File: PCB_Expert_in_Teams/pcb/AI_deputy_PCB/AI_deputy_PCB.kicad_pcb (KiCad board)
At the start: 2 copper layers, 154 parts, among them IC1 DA7280-00FVC, IC2 DA7281-00FVC, IC3 DA7282-00FVC, IC4 IS31AP2005-SLS2-TR, IC5 IS31AP2005-SLS2-TR, IC6 LM25576QMH_NOPB, IC7 CYPD3177-24LQXQ, IC8 FT231XS-R, IC9 PCM5102APWR, J1 Piezo Electric, J10 OUTPUT Haptic B (Neck R), J11 OUTPUT Haptic C (Back), J13 Conn_01x02_Socket, J14 Conn_01x02_Socket, J15 Conn_01x04_Socket, J16 Conn_01x01_Pin, J17 Conn_01x01_Pin, J18 Conn_01x03_Socket, J19 Conn_01x01_Pin, J2 2171790001, J20 Conn_01x01_Pin, J3 Haptic Power and GND, J4 UART, J5 JST CONN from MCU, J6 JTAG, J8 Conn_01x04_Socket, J9 OUTPUT Haptic A (Neck L), Q1 NMOS IRLZ44NPBF, Q2 DMP3098LSD-13, Q4 DMP3098LSD-13, U2 ESP32-WROOM-32UE

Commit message: finished PCB design and gerbers are in directory
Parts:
- removed the D1 at (207.7, 147.9)
- removed the D1 at (101.7, 91.1)
- removed J15: Conn_01x04_Socket, Connector_JST:JST_XH_S4B-XH-A_1x04_P2.50mm_Horizontal
- removed J3: Haptic Power and GND, Connector_JST:JST_XH_S2B-XH-A_1x02_P2.50mm_Horizontal
- removed J5: JST CONN from MCU, Connector_JST:JST_XH_S3B-XH-A_1x03_P2.50mm_Horizontal
- removed J8: Conn_01x04_Socket, Connector_JST:JST_XH_S4B-XH-A-1_1x04_P2.50mm_Horizontal
- removed JP1, JP2: SolderJumper_2_Open, Jumper:SolderJumper-2_P1.3mm_Open_RoundedPad1.0x1.5mm
- removed Q1: NMOS IRLZ44NPBF, Package_TO_SOT_THT:TO-220-3_Horizontal_TabDown
- removed R39, R40: 100k, Resistor_SMD:R_0805_2012Metric_Pad1.20x1.40mm_HandSolder
- removed R53: 3.3k, Resistor_SMD:R_0805_2012Metric_Pad1.20x1.40mm_HandSolder
- removed the R8 at (101.7, 86.3)
- removed the R8 at (207.6, 142.0)
- added C43: 0.1u, Capacitor_SMD:C_0805_2012Metric_Pad1.18x1.45mm_HandSolder, F.Cu at (105.8, 112.0)
- added C60: 10u, Capacitor_SMD:CP_Elec_4x5.4, F.Cu at (99.8, 111.0)
- added C61: 4u7, Capacitor_SMD:C_0805_2012Metric_Pad1.18x1.45mm_HandSolder, F.Cu at (108.0, 107.5)
- added C62: 100n, Capacitor_SMD:C_0805_2012Metric_Pad1.18x1.45mm_HandSolder, F.Cu at (178.1, 81.9)
- added D1: LED, LED_SMD:LED_0805_2012Metric_Pad1.15x1.40mm_HandSolder, F.Cu at (86.9, 86.1)
- added H1: MountingHole, MountingHole:MountingHole_3mm, F.Cu at (195.6, 140.7)
- added H2: MountingHole, MountingHole:MountingHole_3mm, F.Cu at (157.4, 89.7)
- added H3: MountingHole, MountingHole:MountingHole_3mm, F.Cu at (221.9, 85.3)
- added H4: MountingHole, MountingHole:MountingHole_3mm, F.Cu at (73.0, 84.3)
- added H5: MountingHole, MountingHole:MountingHole_3mm, F.Cu at (77.7, 131.3)
- added H6: MountingHole, MountingHole:MountingHole_3mm, F.Cu at (133.3, 125.6)
- added J12: Conn_01x01_Pin, TestPoint:TestPoint_Pad_4.0x4.0mm, F.Cu at (222.0, 103.0)
- added J7: Conn_01x01_Pin, TestPoint:TestPoint_Pad_4.0x4.0mm, F.Cu at (222.0, 112.0)
- added JP3: Jumper_3_Open, Jumper:SolderJumper-3_P1.3mm_Open_Pad1.0x1.5mm_NumberLabels, F.Cu at (130.5, 117.2)
- added JP4: Jumper_3_Open, Jumper:SolderJumper-3_P1.3mm_Open_Pad1.0x1.5mm_NumberLabels, F.Cu at (119.8, 104.0)
- added JP5: Jumper_3_Open, Jumper:SolderJumper-3_P1.3mm_Open_Pad1.0x1.5mm_NumberLabels, F.Cu at (113.2, 141.8)
- added JP6: Jumper_3_Open, Jumper:SolderJumper-3_P1.3mm_Open_Pad1.0x1.5mm_NumberLabels, F.Cu at (126.8, 141.8)
- added L1: 220u, Inductor_SMD:L_Wuerth_WE-PD-Typ-LS, F.Cu at (158.8, 106.5)
- added Q3: Q_NMOS_GDS_IRLZ44N, Package_TO_SOT_THT:TO-220-3_Horizontal_TabDown, F.Cu at (154.7, 133.8)
- added R8: 10k, Resistor_SMD:R_0805_2012Metric_Pad1.20x1.40mm_HandSolder, F.Cu at (91.8, 86.2)
- added S3: L101121MS02Q, EXT_AI_DEPUTY_Library:PWR_SW_L101021MS02Q, F.Cu at (216.0, 141.3)
- added S4: 430773034825, EXT_AI_DEPUTY_Library:430773034825, F.Cu at (143.5, 97.5)
- C46: value 100n -> 1u
- R1: value 3.3k -> 2.7k
- R41: value 10k -> 7.5k
- R47: value 68 -> 100
- R6: value 3.3k -> 10k
- moved R6 108.0 mm to (181.4, 81.8), turned to -90 degrees
- moved R46 95.3 mm to (122.0, 109.0), turned to 90 degrees
- moved R45 89.7 mm to (126.8, 109.0), turned to 90 degrees
- moved R44 84.3 mm to (131.2, 109.0), turned to 90 degrees
- moved J18 80.2 mm to (202.8, 77.7)
- moved C27 68.9 mm to (216.1, 122.8), turned to 90 degrees
- moved C36 58.9 mm to (211.1, 125.4), turned to 90 degrees
- moved C28 55.6 mm to (208.1, 115.9), turned to 90 degrees
- moved R15 53.5 mm to (208.1, 120.4), turned to 90 degrees
- moved R47 53.3 mm to (154.5, 140.2), turned to -90 degrees
- moved R50 52.0 mm to (196.8, 107.0), turned to -90 degrees
- moved C31 50.7 mm to (206.6, 128.9), turned to 0 degrees
- moved R1 50.1 mm to (117.0, 108.8), turned to 180 degrees
- moved C37 49.9 mm to (206.6, 125.4), turned to 90 degrees
- moved R3 49.7 mm to (158.2, 139.6)
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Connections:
- net +BATT renamed +VDC
- C46 pad 1: Net-(IC8-3V3OUT) -> +3V3
- C56 pad 1: Signal Right -> DAC_OUTR
- C57 pad 1: Signal Left -> DAC_OUTL
- IC8 pad 13: Net-(IC8-3V3OUT) -> +3V3
- IC8 pad 14: Net-(IC8-3V3OUT) -> Net-(IC8-RESET#)
- IC8 pad 19: Net-(IC8-CBUS3) -> unconnected-(IC8-CBUS3-Pad19)
- IC9 pad 11: GND -> Net-(IC9-FLT)
- IC9 pad 12: unconnected-(IC9-SCK-Pad12) -> GND
- IC9 pad 16: GND -> Net-(IC9-FMT)
- IC9 pad 17: MUTE -> Net-(IC9-XSMT)
- IC9 pad 18: +3V3 -> Net-(IC9-LDOO)
- R1 pad 1: +3V3 -> GND
- R1 pad 2: NIRQ -> Net-(IC9-XSMT)
- R41 pad 1: MUTE -> Net-(IC9-XSMT)
- R42 pad 2: Signal Right -> DAC_OUTR
- R43 pad 2: Signal Left -> DAC_OUTL
- R5 pad 2: SDA -> NIRQ
- R6 pad 2: SCL -> Net-(IC8-RESET#)
- U2 pad 10: Net-(JP2-A) -> ESPDACOUTL
- U2 pad 11: Net-(JP1-A) -> ESPDACOUTR
- U2 pad 31: PD_INT -> unconnected-(U2-IO19-Pad31)
- U2 pad 37: MUTE -> unconnected-(U2-IO23-Pad37)
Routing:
- net +3V3: track 435.4 -> 879.4 mm, vias 4 -> 19
- net GND: track 0.00 -> 295.8 mm, vias 0 -> 836
- net MCU PWM: track 0.00 -> 90.5 mm, vias 0 -> 2
- net +VDC: track 19.3 -> 100.7 mm
- net SCL: track 67.8 -> 137.7 mm, vias 4 -> 8
- net ESPDACOUTL: track 0.00 -> 65.4 mm, vias 0 -> 2
- net SDA: track 58.7 -> 123.9 mm, vias 5 -> 9
- net ESPDACOUTR: track 0.00 -> 63.0 mm, vias 0 -> 2
- net Signal Left: track 2.28 -> 53.9 mm
- net BOOT: track 9.87 -> 59.8 mm
- net USB_TX: track 7.69 -> 52.3 mm, vias 0 -> 2
- net Net-(Q3-D): track 0.00 -> 40.8 mm
- net NIRQ: track 70.7 -> 109.4 mm, vias 7 -> 9
- net USB_RX: track 7.34 -> 41.9 mm, vias 0 -> 2
- net +BATT: track 0.00 -> 32.7 mm
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- added copper zone on B.Cu, net GND
- added copper zone on F.Cu, net GND
- removed copper zone on F.Cu, net VDC_OUT
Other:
- board outline added: 175 x 71.2 mm
- board text added: "+"
- board text added: "-"
- board text added: "3V3"
- board text added: "3V3 Input Bypass reg."
- board text added: "AUDIO OUT L"
- board text added: "AUDIO OUT R"
- board text added: "BOOT"
- board text added: "BT_LINK"
- board text added: "Battery Input"
- board text added: "DAC"
- board text added: "ESP"
- board text added: "ESP32 JTAG"
- board text added: "ESP32 UART"
- board text added: "Haptic Neck Back"
- board text added: "Haptic Neck L"
- board text added: "Haptic Neck R"
- board text added: "Olfactory Output"
- board text added: "PD I2C"
- board text added: "PD OUT"
- board text added: "PWR SW"
- board text added: "RESET"
- board text added: "RX"
- board text added: "TX"

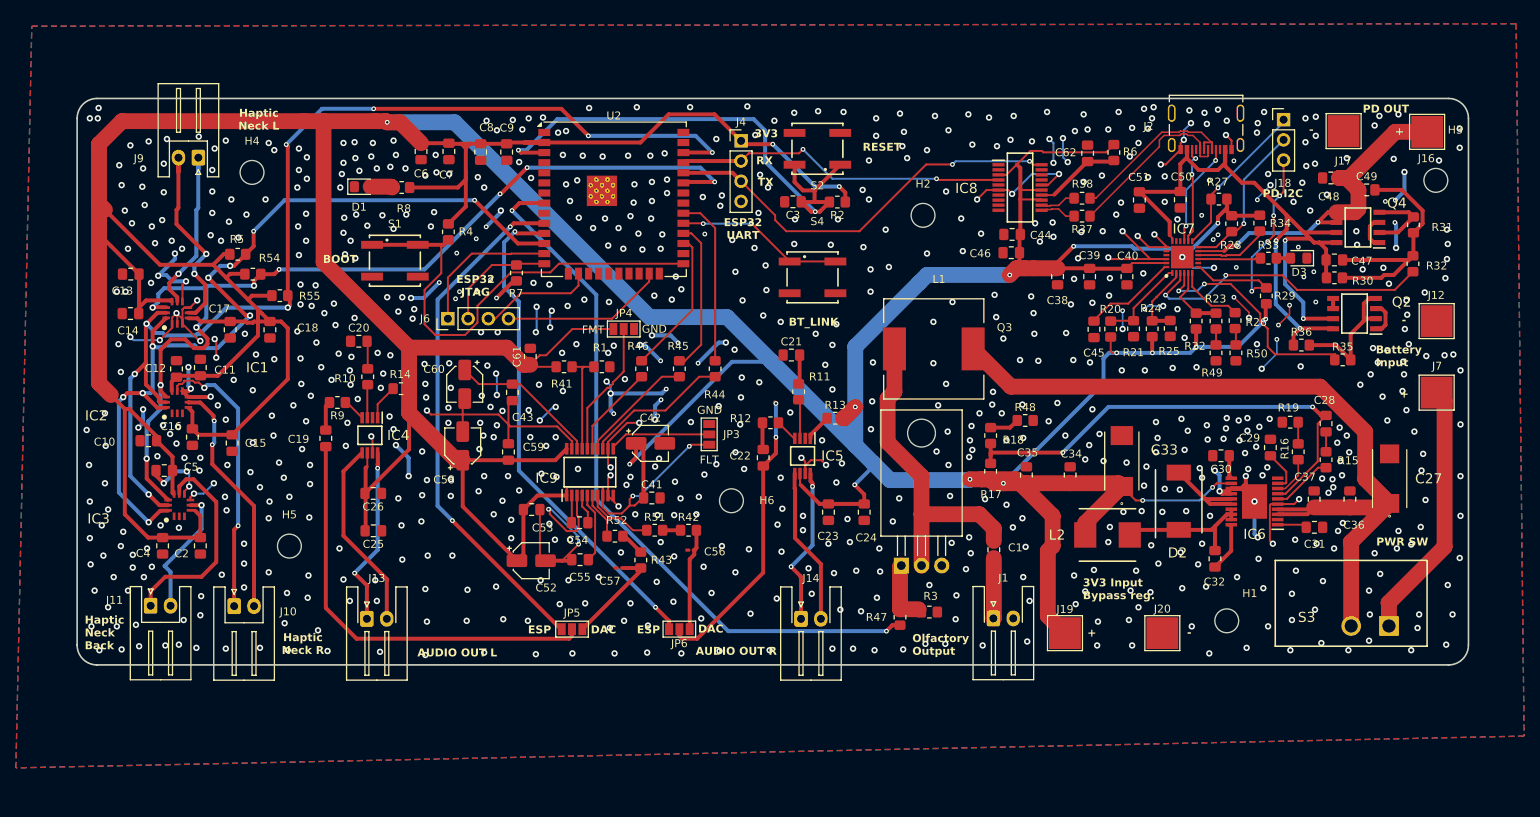
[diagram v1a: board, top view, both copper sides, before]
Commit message: feedback from lawrence implemented in PCB design
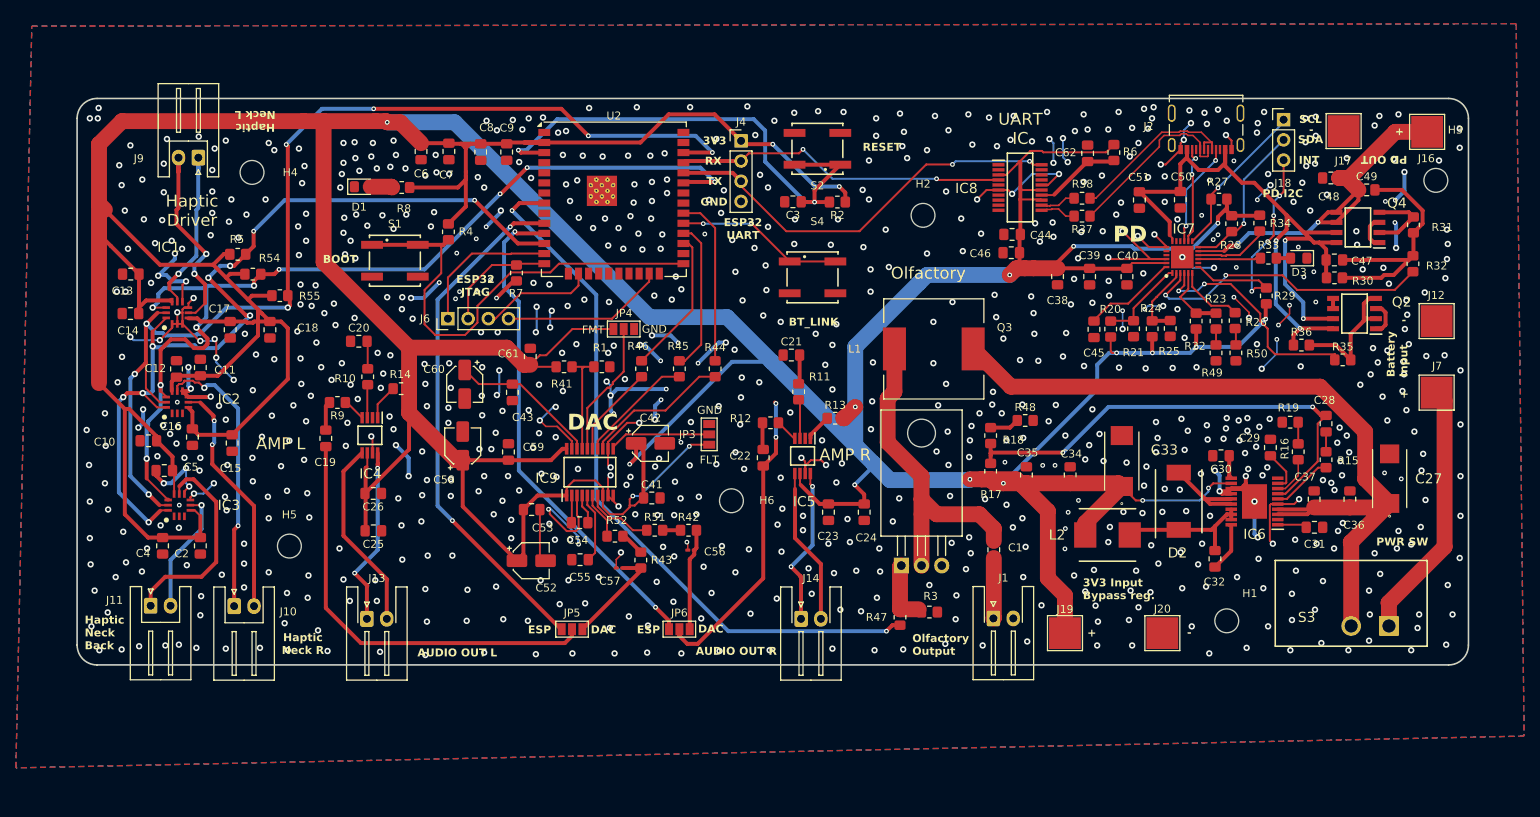
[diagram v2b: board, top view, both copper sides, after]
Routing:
- net GND: track 295.8 -> 274.8 mm, vias 836 -> 819
- net EN_ESP32: track 68.7 -> 64.2 mm
- net VDC_OUT: track 43.9 -> 47.4 mm
- net Signal Right: track 37.1 -> 38.1 mm
- net +3V3: track 879.4 -> 880.2 mm
- net Net-(Q3-D): track 40.8 -> 41.5 mm
- net Net-(IC3-OUTP): track 16.3 -> 15.7 mm
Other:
- board text added: "AMP L"
- board text added: "AMP R"
- board text added: "GND"
- board text added: "Haptic Driver"
- board text added: "INT"
- board text added: "Olfactory"
- board text added: "PD"
- board text added: "SCL"
- board text added: "SDA"
- board text added: "UART IC"
